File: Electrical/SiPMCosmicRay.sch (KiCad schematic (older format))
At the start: 0 parts

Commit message: Small changes...
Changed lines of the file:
@@
-EESchema Schematic File Version 2  date 4/15/2013 9:49:50 PM
+EESchema Schematic File Version 2  date 4/17/2013 7:49:12 PM
 LIBS:power
 LIBS:device
@@
 $Descr A4 11700 8267
 encoding utf-8
-Sheet 1 5
+Sheet 1 6
 Title "Cosmic Ray Detector"
-Date "16 apr 2013"
+Date "17 apr 2013"
 Rev "1A"
 Comp "Ethan Harstad"
@@
 $Sheet
 S 6100 3450 1000 1000
+U 516F2FCF
+F0 "Coincidence" 60
+F1 "Coincidence.sch" 60
+$EndSheet
+$Sheet
+S 7600 3450 1000 1000
 U 516B8E64
 F0 "Power" 60
@@
 F0 "Detector1" 60
 F1 "Detector1.sch" 60
+F2 "HS" O R 4100 2800 60
+F3 "Det" O R 4100 2900 60
 $EndSheet
 $Sheet

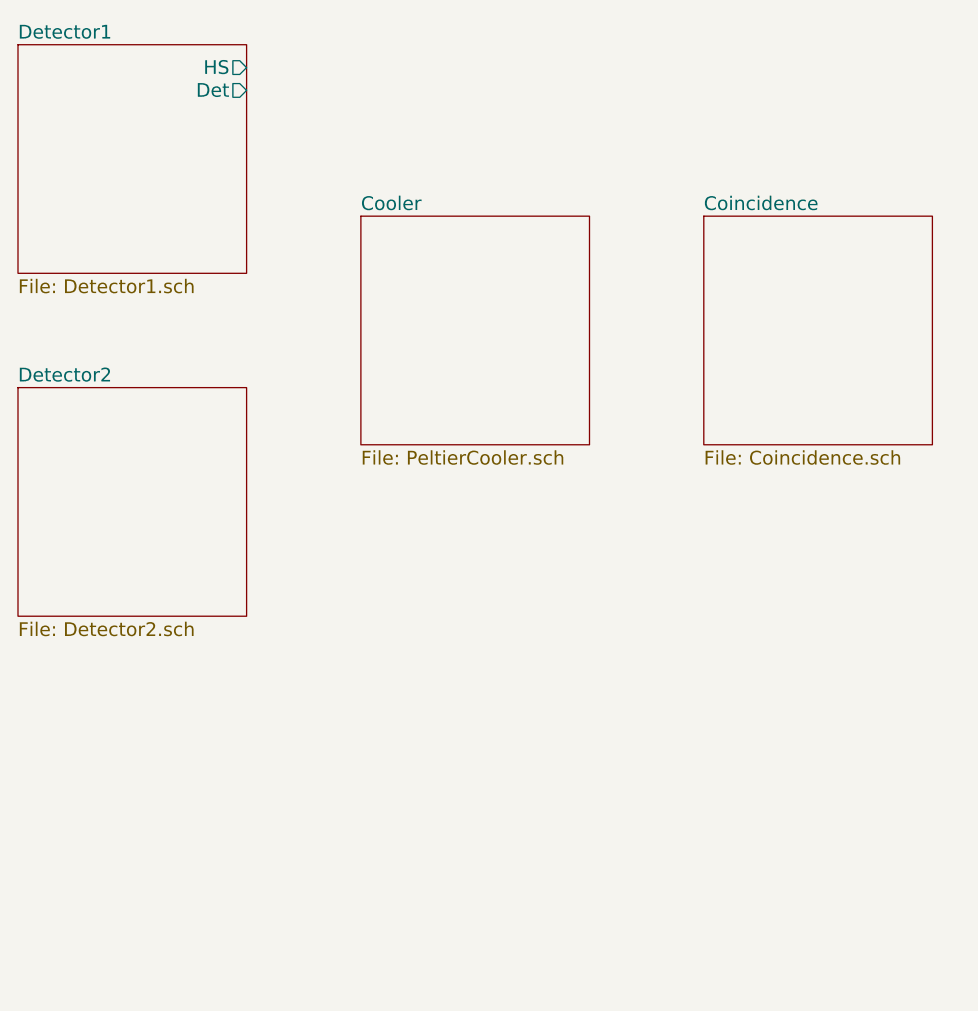
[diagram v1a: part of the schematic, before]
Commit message: Added voltage references and test points
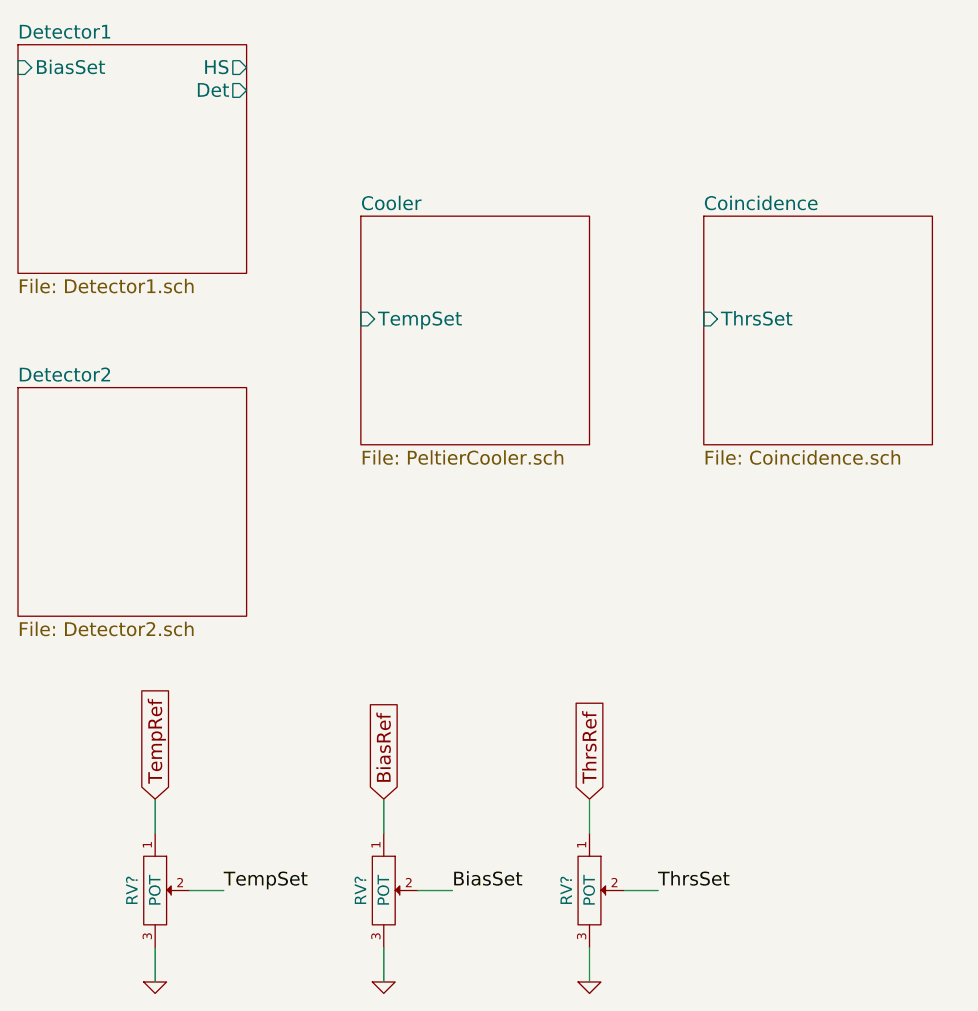
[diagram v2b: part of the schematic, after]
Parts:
- added RV? (x3): POT, symbol POT
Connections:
- new net BiasRef: RV?.1
- new net BiasSet: RV?.2
- new net GND: RV?.3, RV?.3, RV?.3
- new net TempRef: RV?.1
- new net TempSet: RV?.2
- new net ThrsRef: RV?.1
- new net ThrsSet: RV?.2
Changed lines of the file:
@@
-EESchema Schematic File Version 2  date 4/17/2013 7:49:12 PM
+EESchema Schematic File Version 2  date 4/18/2013 6:48:03 PM
 LIBS:power
 LIBS:device
@@
 Sheet 1 6
 Title "Cosmic Ray Detector"
-Date "17 apr 2013"
+Date "18 apr 2013"
 Rev "1A"
 Comp "Ethan Harstad"
@@
 Comment4 ""
 $EndDescr
+Text GLabel 3700 6000 1    60   Input ~ 0
+TempRef
+Wire Wire Line
+	5600 6000 5600 6150
+Wire Wire Line
+	3700 6000 3700 6150
+Wire Wire Line
+	4700 6800 4700 6650
+Wire Wire Line
+	5000 6400 4850 6400
+Wire Wire Line
+	3700 6800 3700 6650
+Wire Wire Line
+	4000 6400 3850 6400
+Wire Wire Line
+	5900 6400 5750 6400
+Wire Wire Line
+	5600 6650 5600 6800
+Wire Wire Line
+	4700 6000 4700 6150
+Text GLabel 5600 6000 1    60   Input ~ 0
+ThrsRef
+Text GLabel 4700 6000 1    60   Input ~ 0
+BiasRef
+$Comp
+L GND #PWR?
+U 1 1 51707B27
+P 4700 6800
+F 0 "#PWR?" H 4700 6800 30  0001 C CNN
+F 1 "GND" H 4700 6730 30  0001 C CNN
+	1    4700 6800
+	1    0    0    -1
+$EndComp
+$Comp
+L GND #PWR?
+U 1 1 51707B22
+P 5600 6800
+F 0 "#PWR?" H 5600 6800 30  0001 C CNN
+F 1 "GND" H 5600 6730 30  0001 C CNN
+	1    5600 6800
+	1    0    0    -1
+$EndComp
+Text Label 5900 6400 0    60   ~ 0
+ThrsSet
+$Comp
+L POT RV?
+U 1 1 51707B04
+P 5600 6400
+F 0 "RV?" H 5600 6300 50  0000 C CNN
+F 1 "POT" H 5600 6400 50  0000 C CNN
+	1    5600 6400
+	0    1    1    0
+$EndComp
+Text Label 5000 6400 0    60   ~ 0
+BiasSet
+$Comp
+L POT RV?
+U 1 1 51707AEB
+P 4700 6400
+F 0 "RV?" H 4700 6300 50  0000 C CNN
+F 1 "POT" H 4700 6400 50  0000 C CNN
+	1    4700 6400
+	0    1    1    0
+$EndComp
+Text Label 4000 6400 0    60   ~ 0
+TempSet
+$Comp
+L GND #PWR?
+U 1 1 51707A98
+P 3700 6800
+F 0 "#PWR?" H 3700 6800 30  0001 C CNN
+F 1 "GND" H 3700 6730 30  0001 C CNN
+	1    3700 6800
+	1    0    0    -1
+$EndComp
+$Comp
+L POT RV?
+U 1 1 51707A88
+P 3700 6400
+F 0 "RV?" H 3700 6300 50  0000 C CNN
+F 1 "POT" H 3700 6400 50  0000 C CNN
+	1    3700 6400
+	0    1    1    0
+$EndComp
 $Sheet
 S 6100 3450 1000 1000
@@
 F0 "Coincidence" 60
 F1 "Coincidence.sch" 60
+F2 "ThrsSet" I L 6100 3900 60
 $EndSheet
 $Sheet
@@
 F2 "HS" O R 4100 2800 60
 F3 "Det" O R 4100 2900 60
+F4 "BiasSet" I L 3100 2800 60
 $EndSheet
 $Sheet
@@
 F0 "Cooler" 60
 F1 "PeltierCooler.sch" 60
+F2 "TempSet" I L 4600 3900 60
 $EndSheet
 Text Notes 9900 6400 0    60   ~ 12

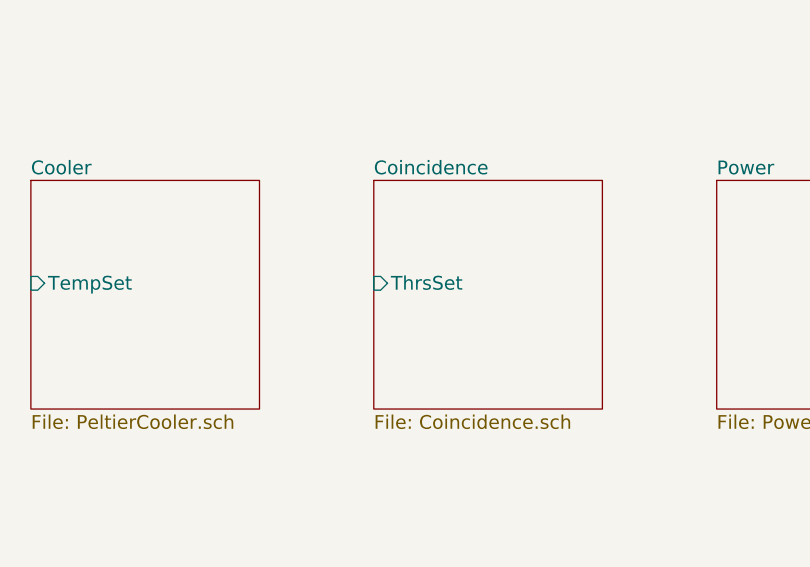
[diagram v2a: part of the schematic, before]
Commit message: Adding schematic annotations to explain functions
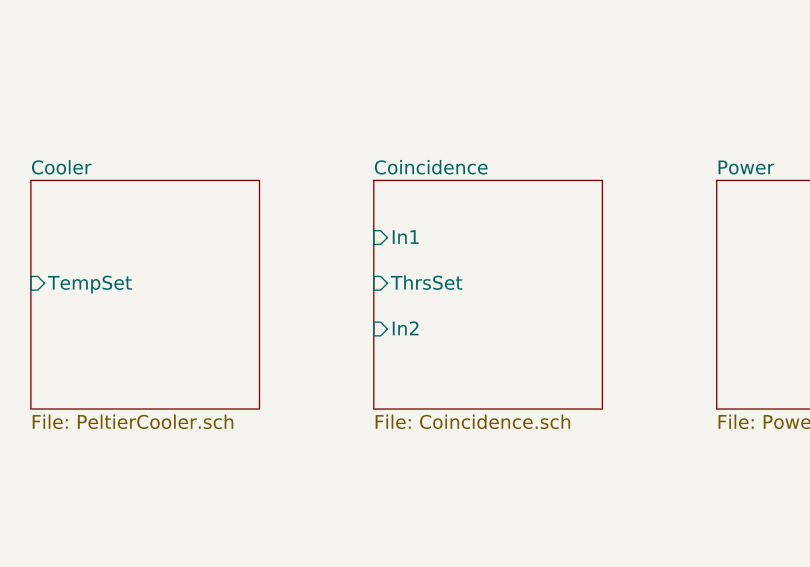
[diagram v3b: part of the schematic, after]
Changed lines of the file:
@@
-EESchema Schematic File Version 2  date 4/18/2013 6:48:03 PM
+EESchema Schematic File Version 2  date 4/18/2013 8:00:54 PM
 LIBS:power
 LIBS:device
@@
 Sheet 1 6
 Title "Cosmic Ray Detector"
-Date "18 apr 2013"
+Date "19 apr 2013"
 Rev "1A"
 Comp "Ethan Harstad"
@@
 F1 "Coincidence.sch" 60
 F2 "ThrsSet" I L 6100 3900 60
+F3 "In2" I L 6100 4100 60
+F4 "In1" I L 6100 3700 60
 $EndSheet
 $Sheet

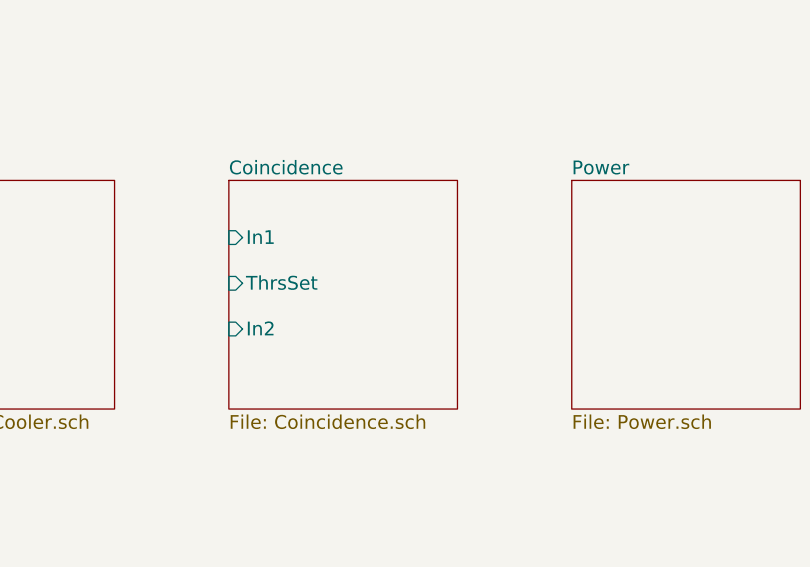
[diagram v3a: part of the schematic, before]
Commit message: Added coincidence circuit to schematic
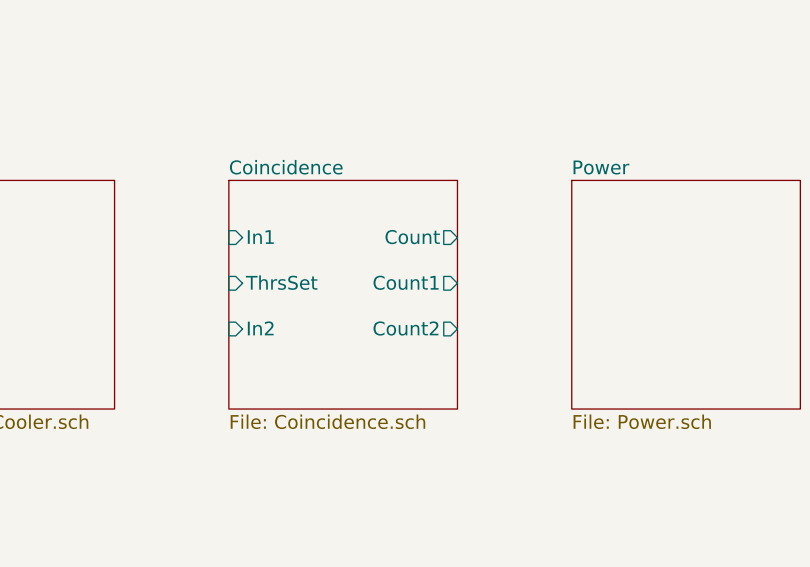
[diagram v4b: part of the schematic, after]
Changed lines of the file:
@@
-EESchema Schematic File Version 2  date 4/18/2013 8:00:54 PM
+EESchema Schematic File Version 2  date 4/18/2013 10:00:18 PM
 LIBS:power
 LIBS:device
@@
 F3 "In2" I L 6100 4100 60
 F4 "In1" I L 6100 3700 60
+F5 "Count" O R 7100 3700 60
+F6 "Count2" O R 7100 4100 60
+F7 "Count1" O R 7100 3900 60
 $EndSheet
 $Sheet
